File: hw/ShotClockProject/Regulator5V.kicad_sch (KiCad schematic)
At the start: 13 parts, among them U2 TPS63000

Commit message: Finshed both schematics
- LED driving transistors are placed
- All connectors on segment display PCB are placed
- All schematic references have been re-configured (autosort on Y axis)
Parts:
- removed R10: 1k5, Resistor_SMD:R_0402_1005Metric, symbol Device:R
- removed R10: 100R, Resistor_SMD:R_0402_1005Metric, symbol Device:R
- added R10: 100R, Resistor_SMD:R_0402_1005Metric, symbol Device:R
- added R10: 1k5, Resistor_SMD:R_0402_1005Metric, symbol Device:R
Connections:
- net GND: now also R10.2
- net batt_in: now also R10.1
- net at D2.1 (K): now also R10.1
- net at C14.1, U2.6 (EN), U2.7 (PS/SYNC)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: now also R10.2

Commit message: Added LCSC Part number
Renamed output folders
Created first output files for REV1
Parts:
- C14: LCSC Part (none) -> C1525; LCSC Part # (none) -> C1525
- C15, C16, C17: LCSC Part (none) -> C96446; LCSC Part # (none) -> C96446
- C18: LCSC Part (none) -> C1559; LCSC Part # (none) -> C1559
- D2: LCSC Part (none) -> C72043; LCSC Part # (none) -> C72043
- L1: LCSC Part (none) -> C404494; LCSC Part # (none) -> C404494
- R10: LCSC Part (none) -> C25076; LCSC Part # (none) -> C25076
- R10: LCSC Part (none) -> C25867; LCSC Part # (none) -> C25867
- R11: LCSC Part (none) -> C144787; LCSC Part # (none) -> C144787
- R12: LCSC Part (none) -> C25745; LCSC Part # (none) -> C25745
- U2: LCSC Part (none) -> C24966; LCSC Part # (none) -> C24966
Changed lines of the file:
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@@
+      (effects (font (size 1.27 1.27)) hide)
+    )
+    (property "LCSC Part #" "" (at 76.2 67.31 0)
+      (effects (font (size 1.27 1.27)) hide)
+    )
+    (property "LCSC Part" "" (at 76.2 67.31 0)
       (effects (font (size 1.27 1.27)) hide)
     )
@@
     )
     (property "Datasheet" "http://www.ti.com/lit/ds/symlink/tps63000.pdf" (at 78.74 34.29 0)
+      (effects (font (size 1.27 1.27)) hide)
+    )
+    (property "LCSC Part #" "C24966" (at 86.36 48.26 0)
+      (effects (font (size 1.27 1.27)) hide)
+    )
+    (property "LCSC Part" "C24966" (at 86.36 48.26 0)
       (effects (font (size 1.27 1.27)) hide)
     )
@@
       (effects (font (size 1.27 1.27)) hide)
     )
+    (property "LCSC Part #" "C96446" (at 48.26 52.07 0)
+      (effects (font (size 1.27 1.27)) hide)
+    )
+    (property "LCSC Part" "C96446" (at 48.26 52.07 0)
+      (effects (font (size 1.27 1.27)) hide)
+    )
     (pin "1")
     (pin "2")
@@
       (effects (font (size 1.27 1.27)) hide)
     )
+    (property "LCSC Part #" "C72043" (at 154.94 45.72 0)
+      (effects (font (size 1.27 1.27)) hide)
+    )
+    (property "LCSC Part" "C72043" (at 154.94 45.72 0)
+      (effects (font (size 1.27 1.27)) hide)
+    )
     (pin "1")
     (pin "2")
@@
     )
     (property "Datasheet" "~" (at 144.78 44.45 0)
+      (effects (font (size 1.27 1.27)) hide)
+    )
+    (property "LCSC Part #" "C96446" (at 144.78 44.45 0)
+      (effects (font (size 1.27 1.27)) hide)
+    )
+    (property "LCSC Part" "C96446" (at 144.78 44.45 0)
       (effects (font (size 1.27 1.27)) hide)
     )
@@
       (effects (font (size 1.27 1.27)) hide)
     )
+    (property "LCSC Part #" "C25076" (at 59.69 41.91 0)
+      (effects (font (size 1.27 1.27)) hide)
+    )
+    (property "LCSC Part" "C25076" (at 59.69 41.91 0)
+      (effects (font (size 1.27 1.27)) hide)
+    )
     (pin "1")
     (pin "2")
@@
       (effects (font (size 1.27 1.27)) hide)
     )
+    (property "LCSC Part #" "C96446" (at 134.62 44.45 0)
+      (effects (font (size 1.27 1.27)) hide)
+    )
+    (property "LCSC Part" "C96446" (at 134.62 44.45 0)
+      (effects (font (size 1.27 1.27)) hide)
+    )
     (pin "1")
     (pin "2")
@@
     )
     (property "Datasheet" "~" (at 154.94 54.61 0)
+      (effects (font (size 1.27 1.27)) hide)
+    )
+    (property "LCSC Part #" "C25867" (at 154.94 54.61 0)
+      (effects (font (size 1.27 1.27)) hide)
+    )
+    (property "LCSC Part" "C25867" (at 154.94 54.61 0)
       (effects (font (size 1.27 1.27)) hide)
     )
@@
       (effects (font (size 1.27 1.27)) hide)
     )
+    (property "LCSC Part #" "C1525" (at 59.69 52.07 0)
+      (effects (font (size 1.27 1.27)) hide)
+    )
+    (property "LCSC Part" "C1525" (at 59.69 52.07 0)
+      (effects (font (size 1.27 1.27)) hide)
+    )
     (pin "1")
     (pin "2")
@@
     )
     (property "Datasheet" "~" (at 102.87 49.53 0)
+      (effects (font (size 1.27 1.27)) hide)
+    )
+    (property "LCSC Part #" "C25745" (at 102.87 49.53 0)
+      (effects (font (size 1.27 1.27)) hide)
+    )
+    (property "LCSC Part" "C25745" (at 102.87 49.53 0)
       (effects (font (size 1.27 1.27)) hide)
     )
@@
       (effects (font (size 1.27 1.27)) hide)
     )
+    (property "LCSC Part #" "C1559" (at 113.03 41.91 0)
+      (effects (font (size 1.27 1.27)) hide)
+    )
+    (property "LCSC Part" "C1559" (at 113.03 41.91 0)
+      (effects (font (size 1.27 1.27)) hide)
+    )
     (pin "1")
     (pin "2")
@@
       (effects (font (size 1.27 1.27)) hide)
     )
+    (property "LCSC Part #" "C404494" (at 73.66 53.34 0)
+      (effects (font (size 1.27 1.27)) hide)
+    )
+    (property "LCSC Part" "C404494" (at 73.66 53.34 0)
+      (effects (font (size 1.27 1.27)) hide)
+    )
     (pin "1")
     (pin "2")
@@
       (effects (font (size 1.27 1.27)) hide)
     )
+    (property "LCSC Part #" "C144787" (at 102.87 41.91 0)
+      (effects (font (size 1.27 1.27)) hide)
+    )
+    (property "LCSC Part" "C144787" (at 102.87 41.91 0)
+      (effects (font (size 1.27 1.27)) hide)
+    )

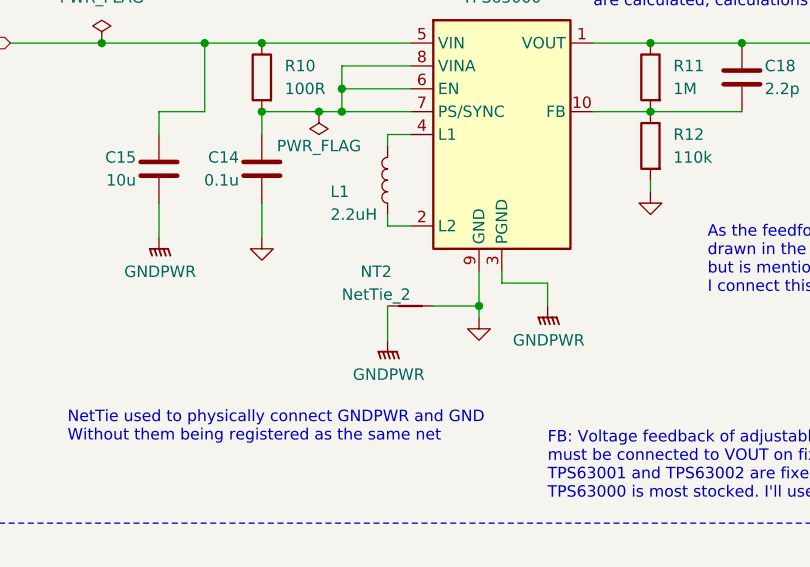
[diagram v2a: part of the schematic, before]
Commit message: Added LCSC part numbers, and changed TPS vias
- Changed the footprint for the TPS regulators, so they don't have 0.2mm vias. Manually placed GND vias next to the footprint.
- Removed NETTIES to get rid of weird across the map connection of GND and GNDPWR.
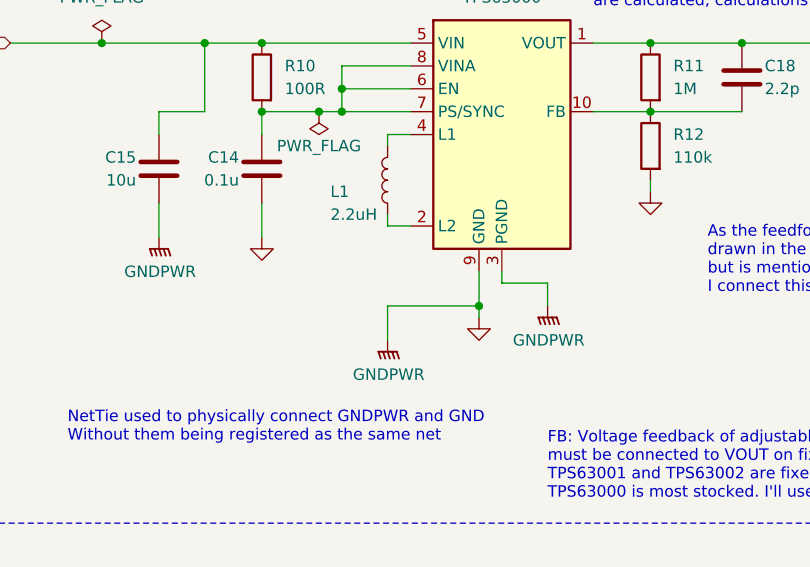
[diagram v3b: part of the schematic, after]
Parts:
- removed NT2: NetTie_2, NetTie:NetTie-2_SMD_Pad2.0mm, symbol Device:NetTie_2
- U2: footprint Package_SON_Altered:Texas_DRC0010J_ThermalVias_Altered -> Package_SON:Texas_DRC0010J
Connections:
- net GNDPWR is gone; now on net GND: C15.2, C16.2, C17.2, U2.11 (PGND), U2.3 (PGND)
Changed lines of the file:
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@@
     (stroke (width 0) (type default))
   )
-  (wire (pts (xy 78.74 67.31) (xy 83.82 67.31))
+  (wire (pts (xy 73.66 67.31) (xy 83.82 67.31))
     (stroke (width 0) (type default))
   )
@@
     )
   )
-  (symbol (lib_id "Device:NetTie_2") (at 76.2 67.31 0) (unit 1)
-    (in_bom no) (on_board yes) (dnp no)
-    (property "Reference" "NT2" (at 72.39 63.5 0)
-      (effects (font (size 1.27 1.27)))
-    )
-    (property "Value" "NetTie_2" (at 72.39 66.04 0)
-      (effects (font (size 1.27 1.27)))
-    )
-    (property "Footprint" "NetTie:NetTie-2_SMD_Pad2.0mm" (at 76.2 67.31 0)
-      (effects (font (size 1.27 1.27)) hide)
-    )
-    (property "Datasheet" "~" (at 76.2 67.31 0)
-      (effects (font (size 1.27 1.27)) hide)
-    )
-    (property "LCSC Part #" "" (at 76.2 67.31 0)
-      (effects (font (size 1.27 1.27)) hide)
-    )
-    (property "LCSC Part" "" (at 76.2 67.31 0)
-      (effects (font (size 1.27 1.27)) hide)
-    )
-    (pin "1")
-    (pin "2")
-    (instances
-      (project "ShotClockProject"
-        (path "/5fd859aa-754d-49c2-9762-3f7ebe3bb64c/17367eb9-0f4d-4017-b1ca-d50430410a5d"
-          (reference "NT2") (unit 1)
-        )
-        (path "/5fd859aa-754d-49c2-9762-3f7ebe3bb64c/83d8d19c-1376-4688-800d-ae057ad1fe11"
-          (reference "NT3") (unit 1)
-        )
-      )
-    )
-  )
   (symbol (lib_id "power:GNDPWR") (at 73.66 71.12 0) (mirror y) (unit 1)
     (in_bom yes) (on_board yes) (dnp no) (fields_autoplaced)
@@
       (effects (font (size 1.27 1.27)))
     )
-    (property "Footprint" "Package_SON_Altered:Texas_DRC0010J_ThermalVias_Altered" (at 107.95 62.23 0)
-      (effects (font (size 1.27 1.27)) hide)
-    )
+    (property "Footprint" "Package_SON:Texas_DRC0010J" (at 107.95 62.23 0)
+      (effects (font (size 1.27 1.27)) hide)
+    )

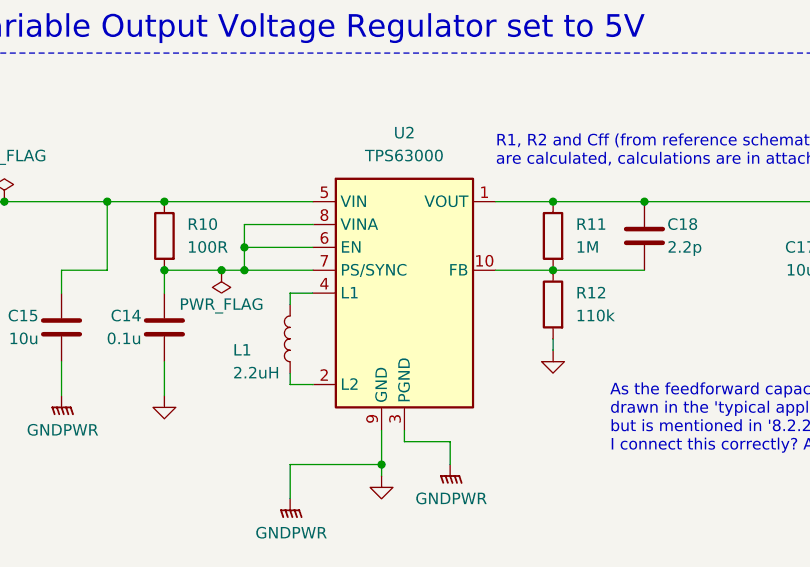
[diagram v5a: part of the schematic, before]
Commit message: Routed V regulators on mainboard
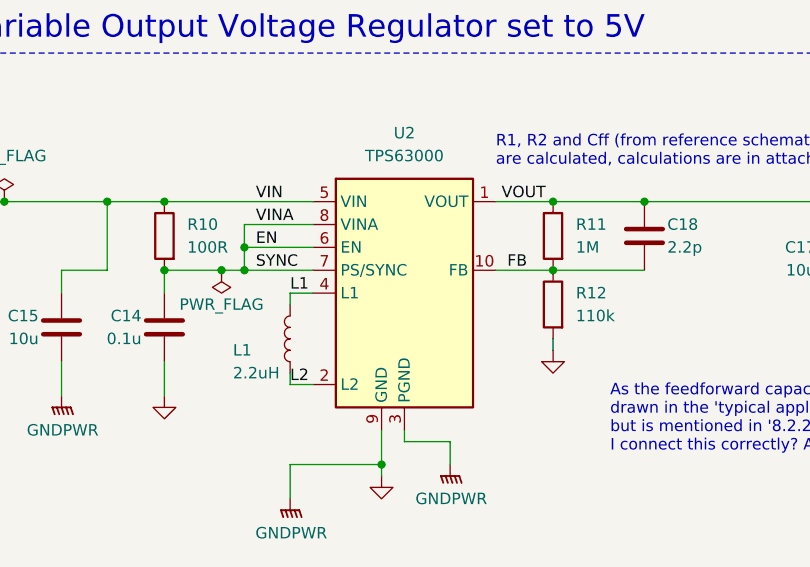
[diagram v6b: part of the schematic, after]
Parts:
- U2: footprint Package_SON:Texas_DRC0010J -> Package_SON_Altered:Texas_DRC0010J_Altered
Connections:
- net FB: now reaches C18.2, R11.2, R12.1, U2.10 (FB)
- net L2: now reaches L1.2, U2.2 (L2)
- net L1: now reaches L1.1, U2.4 (L1)
- net EN: now reaches C14.1, R10.2, U2.6 (EN), U2.7 (PS/SYNC), U2.8 (VINA)
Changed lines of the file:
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@@
     (effects (font (size 2.5 2.5) (color 255 0 0 1)) (justify left bottom))
+  )
+  (label "L1" (at 73.66 48.26 0) (fields_autoplaced)
+    (effects (font (size 1.27 1.27)) (justify left bottom))
+  )
+  (label "FB" (at 97.79 45.72 0) (fields_autoplaced)
+    (effects (font (size 1.27 1.27)) (justify left bottom))
+  )
+  (label "VIN" (at 69.85 38.1 0) (fields_autoplaced)
+    (effects (font (size 1.27 1.27)) (justify left bottom))
+  )
+  (label "VINA" (at 69.85 40.64 0) (fields_autoplaced)
+    (effects (font (size 1.27 1.27)) (justify left bottom))
+  )
+  (label "VOUT" (at 97.155 38.1 0) (fields_autoplaced)
+    (effects (font (size 1.27 1.27)) (justify left bottom))
+  )
+  (label "SYNC" (at 69.85 45.72 0) (fields_autoplaced)
+    (effects (font (size 1.27 1.27)) (justify left bottom))
+  )
+  (label "L2" (at 73.66 58.42 0) (fields_autoplaced)
+    (effects (font (size 1.27 1.27)) (justify left bottom))
+  )
+  (label "EN" (at 69.85 43.18 0) (fields_autoplaced)
+    (effects (font (size 1.27 1.27)) (justify left bottom))
   )
   (hierarchical_label "batt_in" (shape input) (at 31.75 38.1 180) (fields_autoplaced)
@@
       (effects (font (size 1.27 1.27)))
     )
-    (property "Footprint" "Package_SON:Texas_DRC0010J" (at 107.95 62.23 0)
+    (property "Footprint" "Package_SON_Altered:Texas_DRC0010J_Altered" (at 107.95 62.23 0)
       (effects (font (size 1.27 1.27)) hide)
     )

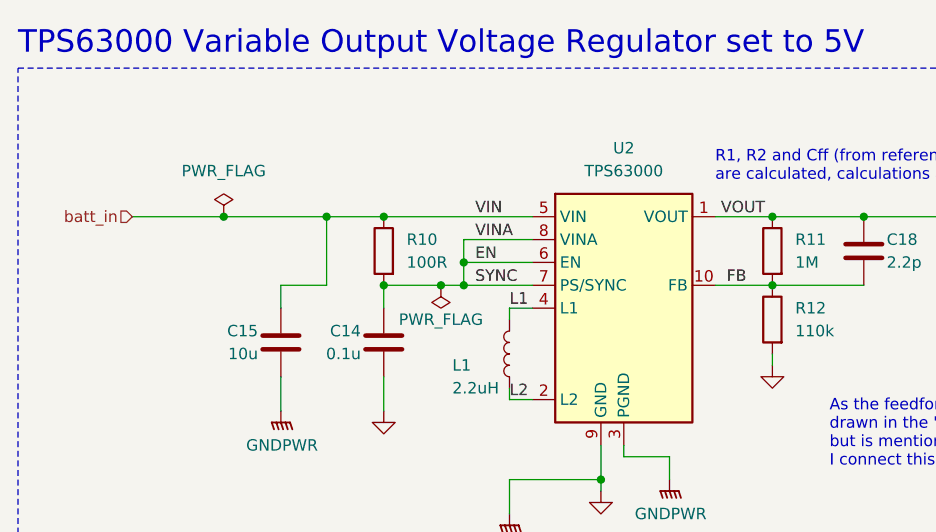
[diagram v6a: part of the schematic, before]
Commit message: Routing on mainboard for LiPo charger
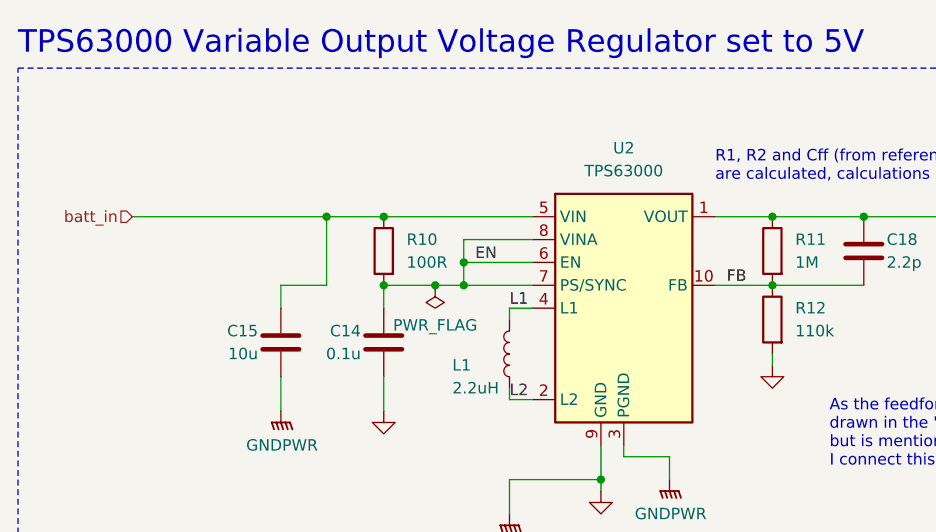
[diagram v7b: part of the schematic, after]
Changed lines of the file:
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@@
   (junction (at 68.58 43.18) (diameter 0) (color 0 0 0 0)
   )
-  (junction (at 66.04 45.72) (diameter 0) (color 0 0 0 0)
-  )
   (junction (at 59.69 45.72) (diameter 0) (color 0 0 0 0)
   )
-  (junction (at 41.91 38.1) (diameter 0) (color 0 0 0 0)
+  (junction (at 65.405 45.72) (diameter 0) (color 0 0 0 0)
   )
   (junction (at 53.34 38.1) (diameter 0) (color 0 0 0 0)
@@
     (stroke (width 0) (type default))
   )
-  (wire (pts (xy 66.04 45.72) (xy 68.58 45.72))
+  (wire (pts (xy 59.69 45.72) (xy 65.405 45.72))
     (stroke (width 0) (type default))
   )
@@
     (stroke (width 0) (type default))
   )
+  (wire (pts (xy 65.405 45.72) (xy 68.58 45.72))
+    (stroke (width 0) (type default))
+  )
   (wire (pts (xy 59.69 38.1) (xy 53.34 38.1))
     (stroke (width 0) (type default))
@@
     (stroke (width 0) (type default))
   )
-  (wire (pts (xy 41.91 38.1) (xy 53.34 38.1))
+  (wire (pts (xy 31.75 38.1) (xy 53.34 38.1))
     (stroke (width 0) (type default))
   )
@@
     (stroke (width 0) (type default))
   )
-  (wire (pts (xy 59.69 45.72) (xy 66.04 45.72))
-    (stroke (width 0) (type default))
-  )
   (wire (pts (xy 73.66 58.42) (xy 73.66 57.15))
-    (stroke (width 0) (type default))
-  )
-  (wire (pts (xy 31.75 38.1) (xy 41.91 38.1))
     (stroke (width 0) (type default))
   )
@@
     (effects (font (size 1.27 1.27)) (justify left bottom))
   )
-  (label "VIN" (at 69.85 38.1 0) (fields_autoplaced)
-    (effects (font (size 1.27 1.27)) (justify left bottom))
-  )
-  (label "VINA" (at 69.85 40.64 0) (fields_autoplaced)
-    (effects (font (size 1.27 1.27)) (justify left bottom))
-  )
-  (label "VOUT" (at 97.155 38.1 0) (fields_autoplaced)
-    (effects (font (size 1.27 1.27)) (justify left bottom))
-  )
-  (label "SYNC" (at 69.85 45.72 0) (fields_autoplaced)
-    (effects (font (size 1.27 1.27)) (justify left bottom))
-  )
   (label "L2" (at 73.66 58.42 0) (fields_autoplaced)
     (effects (font (size 1.27 1.27)) (justify left bottom))
@@
         (path "/5fd859aa-754d-49c2-9762-3f7ebe3bb64c/83d8d19c-1376-4688-800d-ae057ad1fe11"
           (reference "#PWR058") (unit 1)
+        )
+      )
+    )
+  )
+  (symbol (lib_id "power:PWR_FLAG") (at 65.405 45.72 180) (unit 1)
+    (in_bom yes) (on_board yes) (dnp no) (fields_autoplaced)
+    (property "Reference" "#FLG03" (at 65.405 47.625 0)
+      (effects (font (size 1.27 1.27)) hide)
+    )
+    (property "Value" "PWR_FLAG" (at 65.405 50.165 0)
+      (effects (font (size 1.27 1.27)))
+    )
+    (property "Footprint" "" (at 65.405 45.72 0)
+      (effects (font (size 1.27 1.27)) hide)
+    )
+    (property "Datasheet" "~" (at 65.405 45.72 0)
+      (effects (font (size 1.27 1.27)) hide)
+    )
+    (pin "1")
+    (instances
+      (project "ShotClockProject"
+        (path "/5fd859aa-754d-49c2-9762-3f7ebe3bb64c/d287d155-1951-4d4f-8d6c-570f03bc79f5"
+          (reference "#FLG03") (unit 1)
+        )
+        (path "/5fd859aa-754d-49c2-9762-3f7ebe3bb64c/17367eb9-0f4d-4017-b1ca-d50430410a5d"
+          (reference "#FLG04") (unit 1)
+        )
+        (path "/5fd859aa-754d-49c2-9762-3f7ebe3bb64c/83d8d19c-1376-4688-800d-ae057ad1fe11"
+          (reference "#FLG08") (unit 1)
         )
       )
@@
     )
   )
-  (symbol (lib_id "power:PWR_FLAG") (at 66.04 45.72 180) (unit 1)
-    (in_bom yes) (on_board yes) (dnp no)
-    (property "Reference" "#FLG04" (at 66.04 47.625 0)
-      (effects (font (size 1.27 1.27)) hide)
-    )
-    (property "Value" "PWR_FLAG" (at 66.04 49.53 0)
-      (effects (font (size 1.27 1.27)))
-    )
-    (property "Footprint" "" (at 66.04 45.72 0)
-      (effects (font (size 1.27 1.27)) hide)
-    )
-    (property "Datasheet" "~" (at 66.04 45.72 0)
-      (effects (font (size 1.27 1.27)) hide)
-    )
-    (pin "1")
-    (instances
-      (project "ShotClockProject"
-        (path "/5fd859aa-754d-49c2-9762-3f7ebe3bb64c/d287d155-1951-4d4f-8d6c-570f03bc79f5"
-          (reference "#FLG04") (unit 1)
-        )
-        (path "/5fd859aa-754d-49c2-9762-3f7ebe3bb64c/17367eb9-0f4d-4017-b1ca-d50430410a5d"
-          (reference "#FLG08") (unit 1)
-        )
-        (path "/5fd859aa-754d-49c2-9762-3f7ebe3bb64c/83d8d19c-1376-4688-800d-ae057ad1fe11"
-          (reference "#FLG09") (unit 1)
-        )
-      )
-    )
-  )
   (symbol (lib_id "Device:C") (at 48.26 52.07 0) (mirror y) (unit 1)
     (in_bom yes) (on_board yes) (dnp no)
@@
         )
       )
-    )
-  )
-  (symbol (lib_id "power:PWR_FLAG") (at 41.91 38.1 0) (unit 1)
-    (in_bom yes) (on_board yes) (dnp no) (fields_autoplaced)
-    (property "Reference" "#FLG04" (at 41.91 36.195 0)
-      (effects (font (size 1.27 1.27)) hide)
-    )
-    (property "Value" "PWR_FLAG" (at 41.91 33.02 0)
-      (effects (font (size 1.27 1.27)))
-    )
-    (property "Footprint" "" (at 41.91 38.1 0)
-      (effects (font (size 1.27 1.27)) hide)
-    )
-    (property "Datasheet" "~" (at 41.91 38.1 0)
-      (effects (font (size 1.27 1.27)) hide)
-    )
-    (pin "1")
-    (instances
-      (project "ShotClockProject"
-        (path "/5fd859aa-754d-49c2-9762-3f7ebe3bb64c/d287d155-1951-4d4f-8d6c-570f03bc79f5"
-          (reference "#FLG04") (unit 1)
-        )
-        (path "/5fd859aa-754d-49c2-9762-3f7ebe3bb64c/17367eb9-0f4d-4017-b1ca-d50430410a5d"
-          (reference "#FLG07") (unit 1)
-        )
-        (path "/5fd859aa-754d-49c2-9762-3f7ebe3bb64c/83d8d19c-1376-4688-800d-ae057ad1fe11"
-          (reference "#FLG08") (unit 1)
-        )
-      )
